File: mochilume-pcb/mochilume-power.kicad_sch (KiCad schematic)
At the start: 28 parts, among them U1 llcc68_custom_module

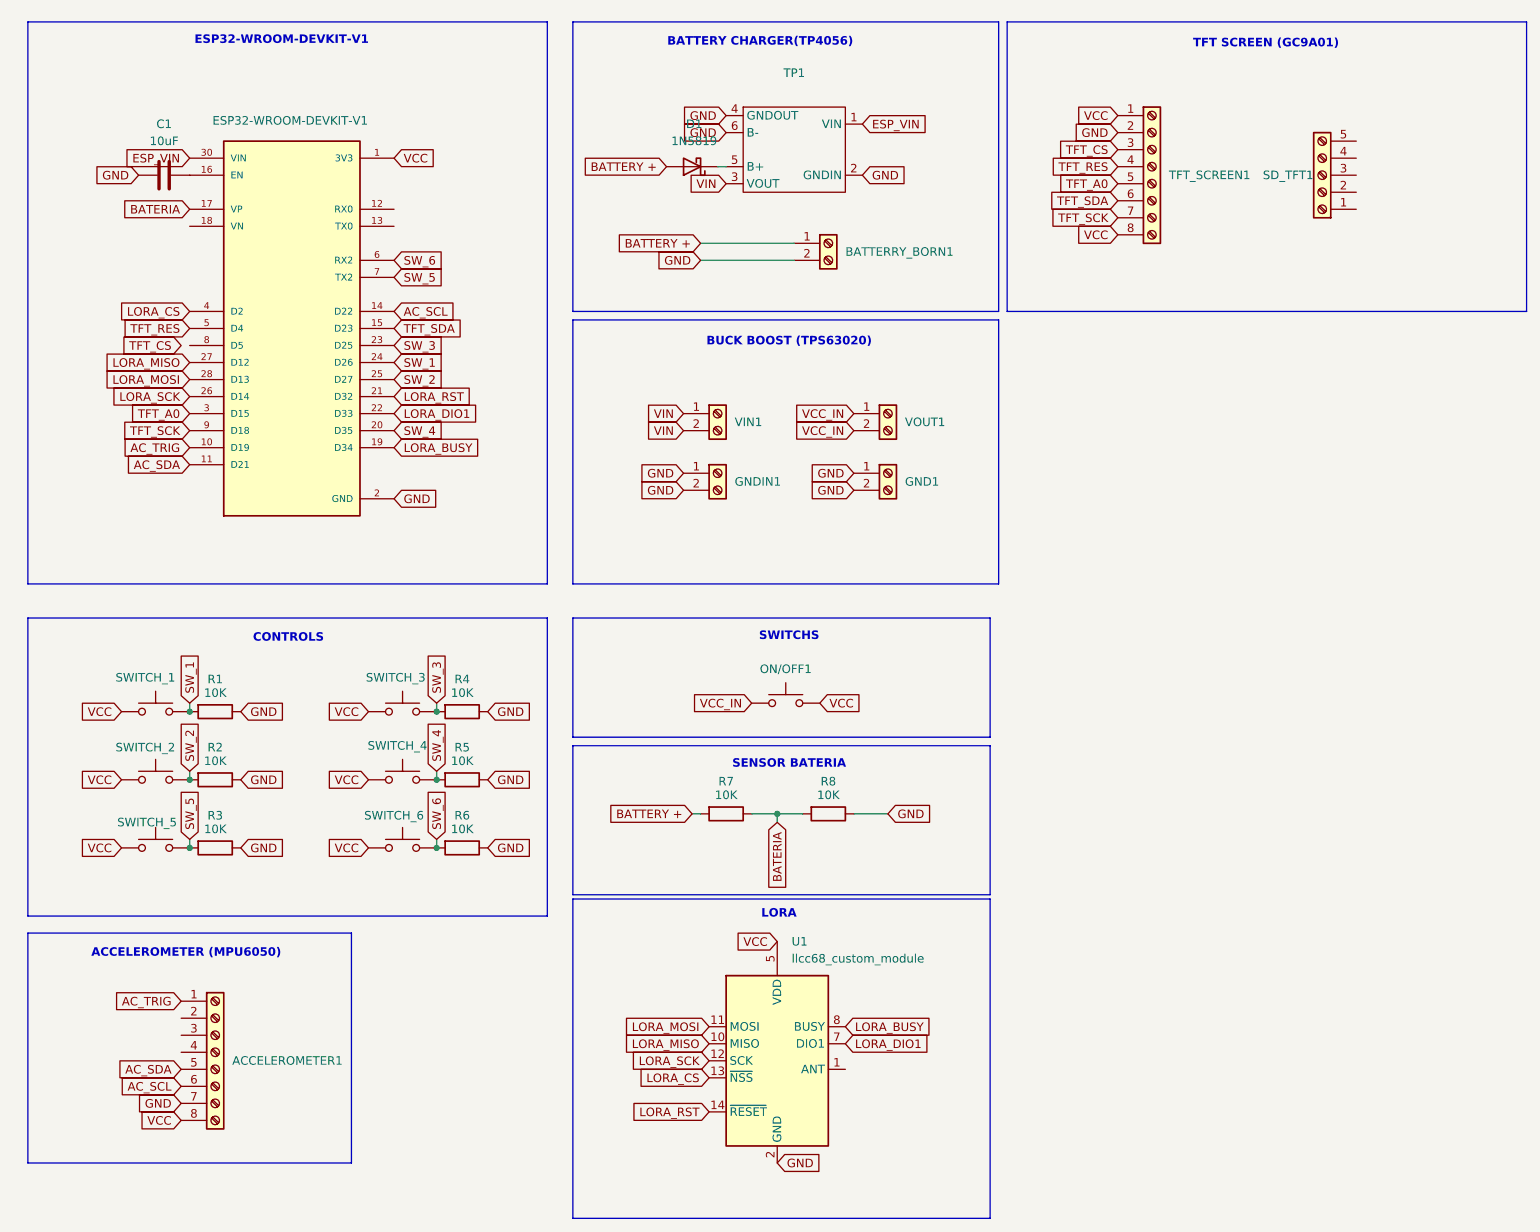
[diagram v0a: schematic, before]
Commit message: feat pcb: add via tracking to power pcb
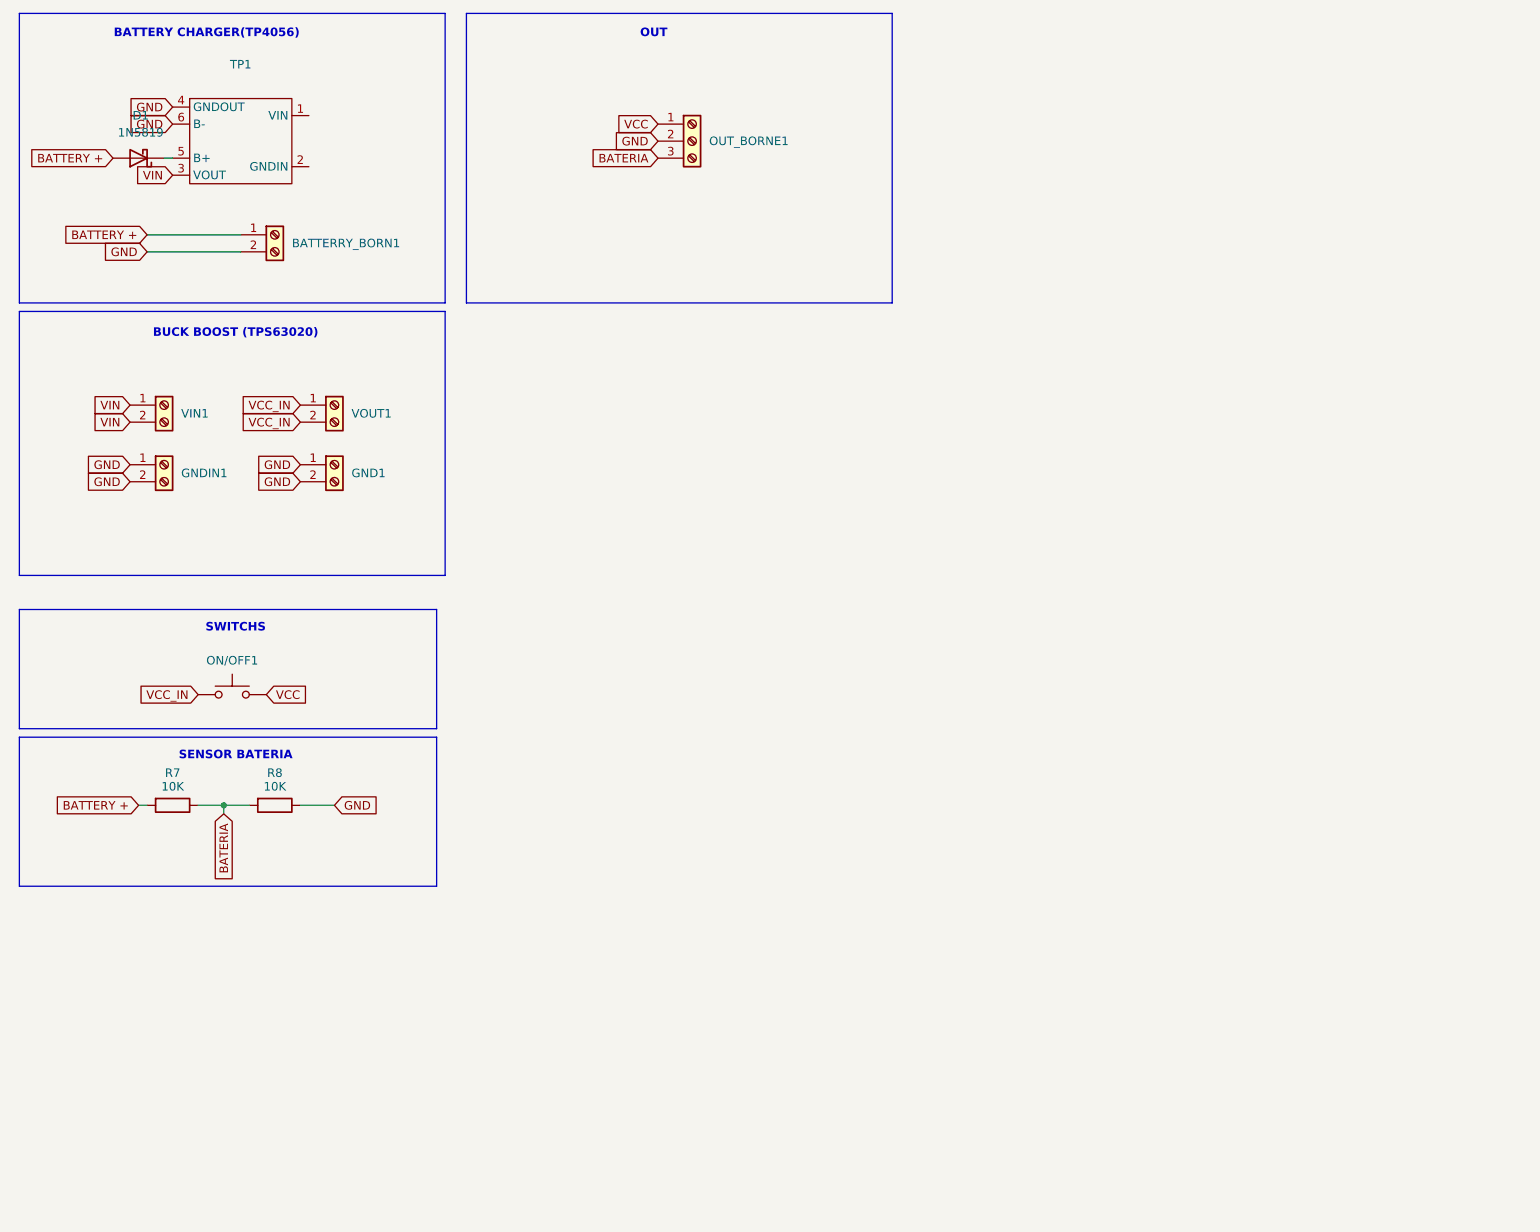
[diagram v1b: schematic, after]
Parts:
- removed ACCELEROMETER1, TFT_SCREEN1: (no value), Connector_PinHeader_2.54mm:PinHeader_1x08_P2.54mm_Vertical, symbol Connector:Screw_Terminal_01x08
- removed C1: 10uF, Capacitor_THT:CP_Radial_D4.0mm_P2.00mm, symbol Device:C
- removed ESP32-WROOM-DEVKIT-V1: (no value), Library:MODULE_ESP32_DEVKIT_V1, symbol ESP32-DEVKIT-V1:ESP32-DEVKIT-V1
- removed R1, R2, R3, R4, R5, R6: 10K, Resistor_THT:R_Axial_DIN0309_L9.0mm_D3.2mm_P15.24mm_Horizontal, symbol Device:R
- removed SD_TFT1: (no value), Connector_PinHeader_2.54mm:PinHeader_1x05_P2.54mm_Vertical, symbol Connector:Screw_Terminal_01x05
- removed SWITCH_1, SWITCH_2, SWITCH_3, SWITCH_4, SWITCH_5, SWITCH_6: (no value), Button_Switch_THT:SW_PUSH_6mm, symbol Switch:SW_Push
- removed U1: llcc68_custom_module, RF_Module:Ai-Thinker-Ra-01-LoRa, symbol custom:llcc68_custom_module
- added OUT_BORNE1: Screw_Terminal_01x03, Connector_PinHeader_2.54mm:PinHeader_1x03_P2.54mm_Vertical, symbol Connector:Screw_Terminal_01x03
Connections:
- net BATERIA: now also OUT_BORNE1.3 (Pin_3)
- net GND: now also OUT_BORNE1.2 (Pin_2); no longer TP1.2 (GNDIN)
- net VCC: now also OUT_BORNE1.1 (Pin_1)
- net ESP_VIN: no longer names the net of TP1.1 (VIN)
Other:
- note added: "OUT"
- note removed: "ACCELEROMETER (MPU6050)"
- note removed: "CONTROLS"
- note removed: "ESP32-WROOM-DEVKIT-V1"
- note removed: "LORA"
- note removed: "TFT SCREEN (GC9A01)"
- moved on the sheet: BATTERRY_BORN1, D1, GND1, GNDIN1, ON/OFF1, R7, R8, TP1, VIN1, VOUT1

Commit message: fix power pcb: fix out bornier footprint
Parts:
- OUT_BORNE1: footprint Connector_PinHeader_2.54mm:PinHeader_1x03_P2.54mm_Vertical -> TerminalBlock:TerminalBlock_MaiXu_MX126-5.0-03P_1x03_P5.00mm
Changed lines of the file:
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@@
 			)
 		)
-		(property "Footprint" "Connector_PinHeader_2.54mm:PinHeader_1x03_P2.54mm_Vertical"
+		(property "Footprint" "TerminalBlock:TerminalBlock_MaiXu_MX126-5.0-03P_1x03_P5.00mm"
 			(at 116.84 36.83 0)
 			(hide yes)

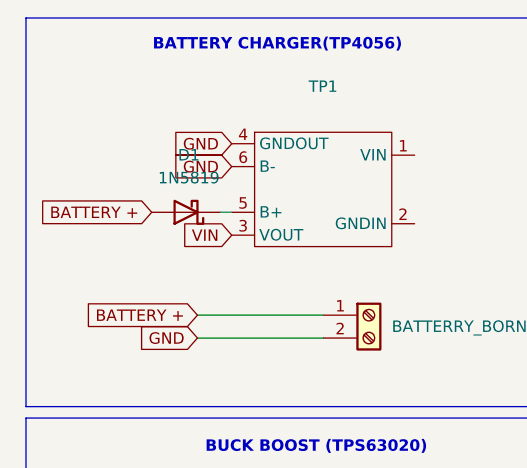
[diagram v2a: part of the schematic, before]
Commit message: fix power pcb: remove diode that disable tpu4056
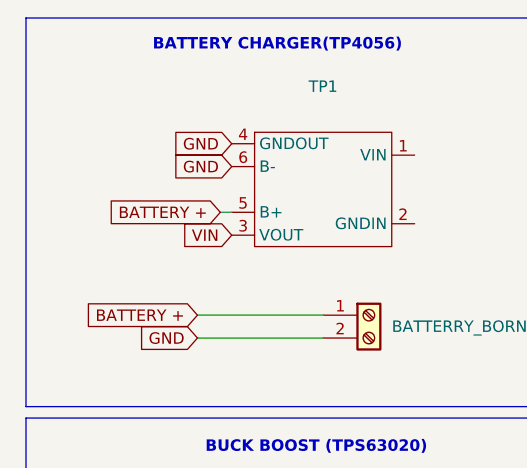
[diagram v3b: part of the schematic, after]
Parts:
- removed D1: 1N5819, Diode_THT:D_DO-41_SOD81_P10.16mm_Horizontal, symbol Diode:1N5819
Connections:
- net BATTERY +: now also TP1.5 (B+)
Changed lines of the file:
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@@
 	(global_label "BATTERY +"
 		(shape input)
-		(at 30.48 39.37 180)
-		(fields_autoplaced yes)
-		(effects
-			(font
-				(size 1.27 1.27)
-			)
-			(justify right)
-		)
-		(property "Intersheetrefs" "${INTERSHEET_REFS}"
-			(at 17.1534 39.37 0)
+		(at 38.1 39.37 180)
+		(fields_autoplaced yes)
+		(effects
+			(font
+				(size 1.27 1.27)
+			)
+			(justify right)
+		)
+		(property "Intersheetrefs" "${INTERSHEET_REFS}"
+			(at 24.7734 39.37 0)
 			(hide yes)
 			(show_name no)
@@
 					(unit 1)
 				)
-			)
-		)
-	)
-	(symbol
-		(lib_id "Diode:1N5819")
-		(at 34.29 39.37 180)
-		(unit 1)
-		(body_style 1)
-		(exclude_from_sim no)
-		(in_bom yes)
-		(on_board yes)
-		(in_pos_files yes)
-		(dnp no)
-		(fields_autoplaced yes)
-		(property "Reference" "D1"
-			(at 34.6075 33.02 0)
-			(show_name no)
-			(do_not_autoplace no)
-			(effects
-				(font
-					(size 1.27 1.27)
-				)
-			)
-		)
-		(property "Value" "1N5819"
-			(at 34.6075 35.56 0)
-			(show_name no)
-			(do_not_autoplace no)
-			(effects
-				(font
-					(size 1.27 1.27)
-				)
-			)
-		)
-		(property "Footprint" "Diode_THT:D_DO-41_SOD81_P10.16mm_Horizontal"
-			(at 34.29 34.925 0)
-			(hide yes)
-			(show_name no)
-			(do_not_autoplace no)
-			(effects
-				(font
-					(size 1.27 1.27)
-				)
-			)
-		)
-		(property "Datasheet" "http://www.vishay.com/docs/88525/1n5817.pdf"
-			(at 34.29 39.37 0)
-			(hide yes)
-			(show_name no)
-			(do_not_autoplace no)
-			(effects
-				(font
-					(size 1.27 1.27)
-				)
-			)
-		)
-		(property "Description" "40V 1A Schottky Barrier Rectifier Diode, DO-41"
-			(at 34.29 39.37 0)
-			(hide yes)
-			(show_name no)
-			(do_not_autoplace no)
-			(effects
-				(font
-					(size 1.27 1.27)
-				)
-			)
-		)
-		(pin "2"
-		)
-		(pin "1"
-		)
-		(instances
-			(project "mochilume-power"
-				(path "/6764fa8e-f873-49cf-a9f0-daca6a1db35f"
-					(reference "D1")
-					(unit 1)
-				)
